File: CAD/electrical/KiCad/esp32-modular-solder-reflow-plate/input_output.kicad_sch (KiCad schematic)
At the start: 65 parts, among them J5 Heater, J6 PWR_IN, Q3 BUZ_CTL

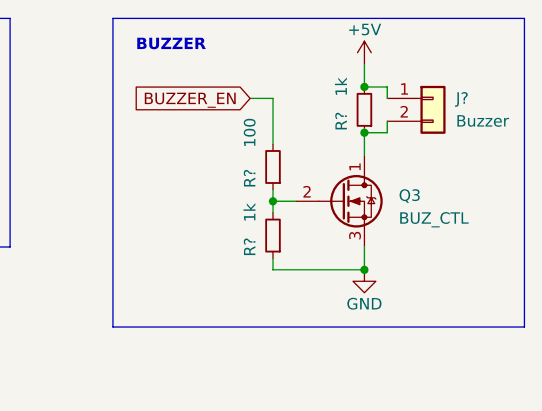
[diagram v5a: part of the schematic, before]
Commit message: - cad: added bypass cap for the buzzer
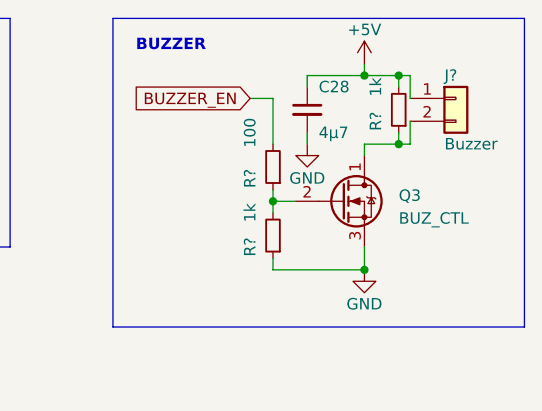
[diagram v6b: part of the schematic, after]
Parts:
- added C28: 4µ7, Capacitor_SMD:C_0603_1608Metric_Pad1.08x0.95mm_HandSolder, symbol Device:C_Small
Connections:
- net +5V: now also C28.1
- net GND: now also C28.2
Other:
- moved on the sheet: J?, R?
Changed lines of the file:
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@@
   (junction (at 43.18 34.29) (diameter 0) (color 0 0 0 0)
   )
+  (junction (at 265.43 21.59) (diameter 0) (color 0 0 0 0)
+  )
   (junction (at 72.39 114.3) (diameter 0) (color 0 0 0 0)
   )
@@
   (junction (at 43.18 24.13) (diameter 0) (color 0 0 0 0)
   )
+  (junction (at 261.62 21.59) (diameter 0) (color 0 0 0 0)
+  )
   (junction (at 72.39 24.13) (diameter 0) (color 0 0 0 0)
   )
@@
   (junction (at 81.28 76.2) (diameter 0) (color 0 0 0 0)
   )
+  (junction (at 265.43 29.21) (diameter 0) (color 0 0 0 0)
+  )
   (junction (at 78.74 114.3) (diameter 0) (color 0 0 0 0)
   )
@@
   (junction (at 132.08 187.96) (diameter 0) (color 0 0 0 0)
   )
-  (junction (at 261.62 22.86) (diameter 0) (color 0 0 0 0)
-  )
   (junction (at 139.7 182.88) (diameter 0) (color 0 0 0 0)
   )
-  (junction (at 261.62 27.94) (diameter 0) (color 0 0 0 0)
-  )
   (junction (at 72.39 34.29) (diameter 0) (color 0 0 0 0)
   )
@@
     (stroke (width 0) (type default))
   )
-  (wire (pts (xy 261.62 22.86) (xy 264.16 22.86))
-    (stroke (width 0) (type default))
-  )
   (wire (pts (xy 71.12 34.29) (xy 72.39 34.29))
     (stroke (width 0) (type default))
@@
     (stroke (width 0) (type default))
   )
-  (wire (pts (xy 264.16 26.67) (xy 264.16 27.94))
+  (wire (pts (xy 266.7 26.67) (xy 266.7 29.21))
     (stroke (width 0) (type default))
   )
@@
     (stroke (width 0) (type default))
   )
+  (wire (pts (xy 255.27 27.94) (xy 255.27 29.21))
+    (stroke (width 0) (type default))
+  )
   (wire (pts (xy 97.79 95.25) (xy 63.5 95.25))
     (stroke (width 0) (type default))
@@
     (stroke (width 0) (type default))
   )
+  (wire (pts (xy 265.43 21.59) (xy 265.43 22.86))
+    (stroke (width 0) (type default))
+  )
   (polyline (pts (xy 233.68 15.24) (xy 279.4 15.24))
     (stroke (width 0) (type default))
@@
     (stroke (width 0) (type default))
   )
+  (wire (pts (xy 265.43 21.59) (xy 266.7 21.59))
+    (stroke (width 0) (type default))
+  )
   (polyline (pts (xy 110.49 69.85) (xy 15.24 69.85))
     (stroke (width 0) (type default))
@@
     (stroke (width 0) (type default))
   )
-  (wire (pts (xy 261.62 20.32) (xy 261.62 22.86))
-    (stroke (width 0) (type default))
-  )
   (wire (pts (xy 118.11 36.83) (xy 118.11 34.29))
     (stroke (width 0) (type default))
@@
     (stroke (width 0) (type default))
   )
-  (wire (pts (xy 261.62 27.94) (xy 264.16 27.94))
-    (stroke (width 0) (type default))
-  )
   (wire (pts (xy 36.83 151.13) (xy 39.37 151.13))
     (stroke (width 0) (type default))
@@
     (stroke (width 0) (type default))
   )
+  (wire (pts (xy 255.27 22.86) (xy 255.27 21.59))
+    (stroke (width 0) (type default))
+  )
   (wire (pts (xy 68.58 187.96) (xy 76.2 187.96))
     (stroke (width 0) (type default))
@@
     (stroke (width 0) (type default))
   )
+  (wire (pts (xy 255.27 21.59) (xy 261.62 21.59))
+    (stroke (width 0) (type default))
+  )
   (wire (pts (xy 209.55 21.59) (xy 217.17 21.59))
     (stroke (width 0) (type default))
@@
     (stroke (width 0) (type default))
   )
-  (wire (pts (xy 264.16 22.86) (xy 264.16 24.13))
+  (wire (pts (xy 266.7 21.59) (xy 266.7 24.13))
     (stroke (width 0) (type default))
   )
@@
     (stroke (width 0) (type default))
   )
+  (wire (pts (xy 265.43 29.21) (xy 261.62 29.21))
+    (stroke (width 0) (type default))
+  )
   (wire (pts (xy 118.11 34.29) (xy 120.65 34.29))
     (stroke (width 0) (type default))
@@
     (stroke (width 0) (type default))
   )
-  (wire (pts (xy 261.62 27.94) (xy 261.62 30.48))
+  (wire (pts (xy 261.62 29.21) (xy 261.62 30.48))
     (stroke (width 0) (type default))
   )
@@
     (stroke (width 0) (type default))
   )
+  (wire (pts (xy 261.62 21.59) (xy 265.43 21.59))
+    (stroke (width 0) (type default))
+  )
   (wire (pts (xy 27.94 127) (xy 27.94 134.62))
     (stroke (width 0) (type default))
@@
     (stroke (width 0) (type default))
   )
+  (wire (pts (xy 265.43 29.21) (xy 265.43 27.94))
+    (stroke (width 0) (type default))
+  )
   (wire (pts (xy 81.28 97.79) (xy 63.5 97.79))
     (stroke (width 0) (type default))
@@
     (stroke (width 0) (type default))
   )
+  (wire (pts (xy 265.43 29.21) (xy 266.7 29.21))
+    (stroke (width 0) (type default))
+  )
   (wire (pts (xy 97.79 90.17) (xy 78.74 90.17))
     (stroke (width 0) (type default))
@@
     (stroke (width 0) (type default))
   )
+  (wire (pts (xy 261.62 21.59) (xy 261.62 20.32))
+    (stroke (width 0) (type default))
+  )
   (wire (pts (xy 76.2 187.96) (xy 76.2 186.69))
     (stroke (width 0) (type default))
@@
     )
   )
+  (symbol (lib_id "Device:C_Small") (at 255.27 25.4 0) (unit 1)
+    (in_bom yes) (on_board yes) (dnp no)
+    (property "Reference" "C28" (at 256.54 22.86 0)
+      (effects (font (size 1.27 1.27)) (justify left))
+    )
+    (property "Value" "4µ7" (at 256.54 27.94 0)
+      (effects (font (size 1.27 1.27)) (justify left))
+    )
+    (property "Footprint" "Capacitor_SMD:C_0603_1608Metric_Pad1.08x0.95mm_HandSolder" (at 255.27 25.4 0)
+      (effects (font (size 1.27 1.27)) hide)
+    )
+    (property "Datasheet" "~" (at 255.27 25.4 0)
+      (effects (font (size 1.27 1.27)) hide)
+    )
+    (pin "1")
+    (pin "2")
+    (instances
+      (project "esp32-modular-solder-reflow-plate"
+        (path "/33f3a99a-8df0-41a5-be2d-1e3400ca68bb/9103847b-7285-41f5-846d-96de7eb793c2"
+          (reference "C28") (unit 1)
+        )
+      )
+    )
+  )
   (symbol (lib_id "power:+5V") (at 191.77 36.83 0) (unit 1)
     (in_bom yes) (on_board yes) (dnp no) (fields_autoplaced)
@@
   (symbol (lib_id "power:+3V3") (at 261.62 20.32 0) (unit 1)
     (in_bom yes) (on_board yes) (dnp no) (fields_autoplaced)
-    (property "Reference" "#PWR049" (at 261.62 24.13 0)
+    (property "Reference" "#PWR050" (at 261.62 24.13 0)
       (effects (font (size 1.27 1.27)) hide)
     )
@@
       (project "esp32-modular-solder-reflow-plate"
         (path "/33f3a99a-8df0-41a5-be2d-1e3400ca68bb/9103847b-7285-41f5-846d-96de7eb793c2"
-          (reference "#PWR049") (unit 1)
+          (reference "#PWR050") (unit 1)
         )
       )
@@
     )
   )
-  (symbol (lib_id "Device:R_Small") (at 261.62 25.4 180) (unit 1)
+  (symbol (lib_id "Device:R_Small") (at 265.43 25.4 180) (unit 1)
     (in_bom yes) (on_board yes) (dnp no)
-    (property "Reference" "R?" (at 259.08 26.67 90)
+    (property "Reference" "R?" (at 262.89 26.67 90)
       (effects (font (size 1.27 1.27)))
     )
-    (property "Value" "1k" (at 259.08 22.86 90)
+    (property "Value" "1k" (at 262.89 22.86 90)
       (effects (font (size 1.27 1.27)))
     )
-    (property "Footprint" "Resistor_SMD:R_0603_1608Metric_Pad0.98x0.95mm_HandSolder" (at 261.62 25.4 0)
+    (property "Footprint" "Resistor_SMD:R_0603_1608Metric_Pad0.98x0.95mm_HandSolder" (at 265.43 25.4 0)
       (effects (font (size 1.27 1.27)) hide)
     )
-    (property "Datasheet" "~" (at 261.62 25.4 0)
+    (property "Datasheet" "~" (at 265.43 25.4 0)
       (effects (font (size 1.27 1.27)) hide)
     )
@@
     )
   )
-  (symbol (lib_id "Connector_Generic:Conn_01x02") (at 269.24 24.13 0) (unit 1)
+  (symbol (lib_id "Connector_Generic:Conn_01x02") (at 271.78 24.13 0) (unit 1)
     (in_bom yes) (on_board yes) (dnp no)
-    (property "Reference" "J?" (at 271.78 24.13 0)
+    (property "Reference" "J?" (at 270.51 21.59 0)
       (effects (font (size 1.27 1.27)) (justify left))
     )
-    (property "Value" "Buzzer" (at 271.78 26.67 0)
+    (property "Value" "Buzzer" (at 270.51 29.21 0)
       (effects (font (size 1.27 1.27)) (justify left))
     )
-    (property "Footprint" "Connector_JST:JST_XH_B2B-XH-A_1x02_P2.50mm_Vertical" (at 269.24 24.13 0)
+    (property "Footprint" "Connector_JST:JST_XH_B2B-XH-A_1x02_P2.50mm_Vertical" (at 271.78 24.13 0)
       (effects (font (size 1.27 1.27)) hide)
     )
-    (property "Datasheet" "~" (at 269.24 24.13 0)
+    (property "Datasheet" "~" (at 271.78 24.13 0)
       (effects (font (size 1.27 1.27)) hide)
     )
@@
     )
   )
+  (symbol (lib_id "power:GND") (at 255.27 29.21 0) (unit 1)
+    (in_bom yes) (on_board yes) (dnp no)
+    (property "Reference" "#PWR?" (at 255.27 35.56 0)
+      (effects (font (size 1.27 1.27)) hide)
+    )
+    (property "Value" "GND" (at 255.27 33.02 0)
+      (effects (font (size 1.27 1.27)))
+    )
+    (property "Footprint" "" (at 255.27 29.21 0)
+      (effects (font (size 1.27 1.27)) hide)
+    )
+    (property "Datasheet" "" (at 255.27 29.21 0)
+      (effects (font (size 1.27 1.27)) hide)
+    )
+    (pin "1")
+    (instances
+      (project "esp32-modular-solder-reflow-plate"
+        (path "/33f3a99a-8df0-41a5-be2d-1e3400ca68bb"
+          (reference "#PWR?") (unit 1)
+        )
+        (path "/33f3a99a-8df0-41a5-be2d-1e3400ca68bb/9103847b-7285-41f5-846d-96de7eb793c2"
+          (reference "#PWR049") (unit 1)
+        )
+      )
+    )
+  )
   (symbol (lib_id "Device:R_Small") (at 251.46 39.37 180) (unit 1)
     (in_bom yes) (on_board yes) (dnp no)
@@
         )
         (path "/33f3a99a-8df0-41a5-be2d-1e3400ca68bb/9103847b-7285-41f5-846d-96de7eb793c2"
-          (reference "#PWR050") (unit 1)
+          (reference "#PWR051") (unit 1)
         )
       )

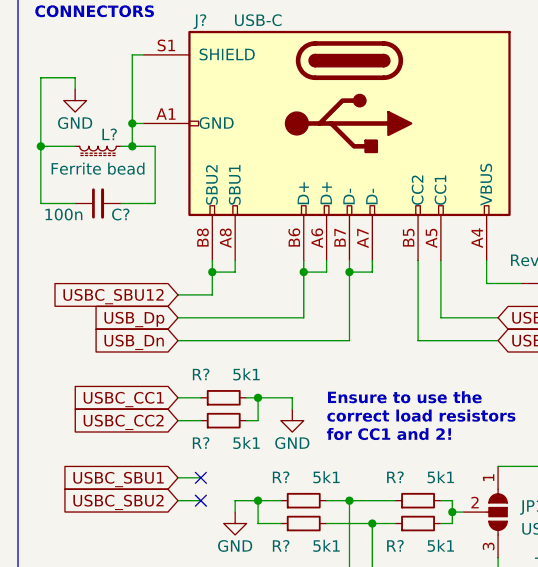
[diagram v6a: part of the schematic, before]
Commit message: - cad: fixed usb c sbu pins; improved usb c slot routing
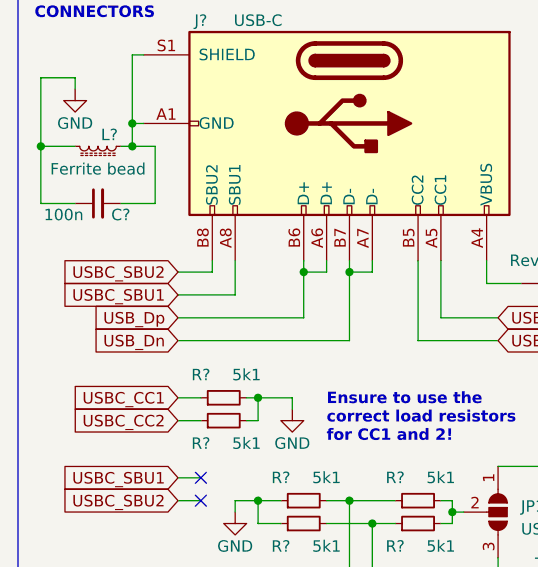
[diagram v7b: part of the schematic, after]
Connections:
- net USBC_SBU1: now also J?.A8 (SBU1)
- net USBC_SBU2: now also J?.B8 (SBU2)
- removed net USBC_SBU12: J?.A8 (SBU1), J?.B8 (SBU2)
